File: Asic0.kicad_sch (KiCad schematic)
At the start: 18 parts, among them U2 BM1370_mode1

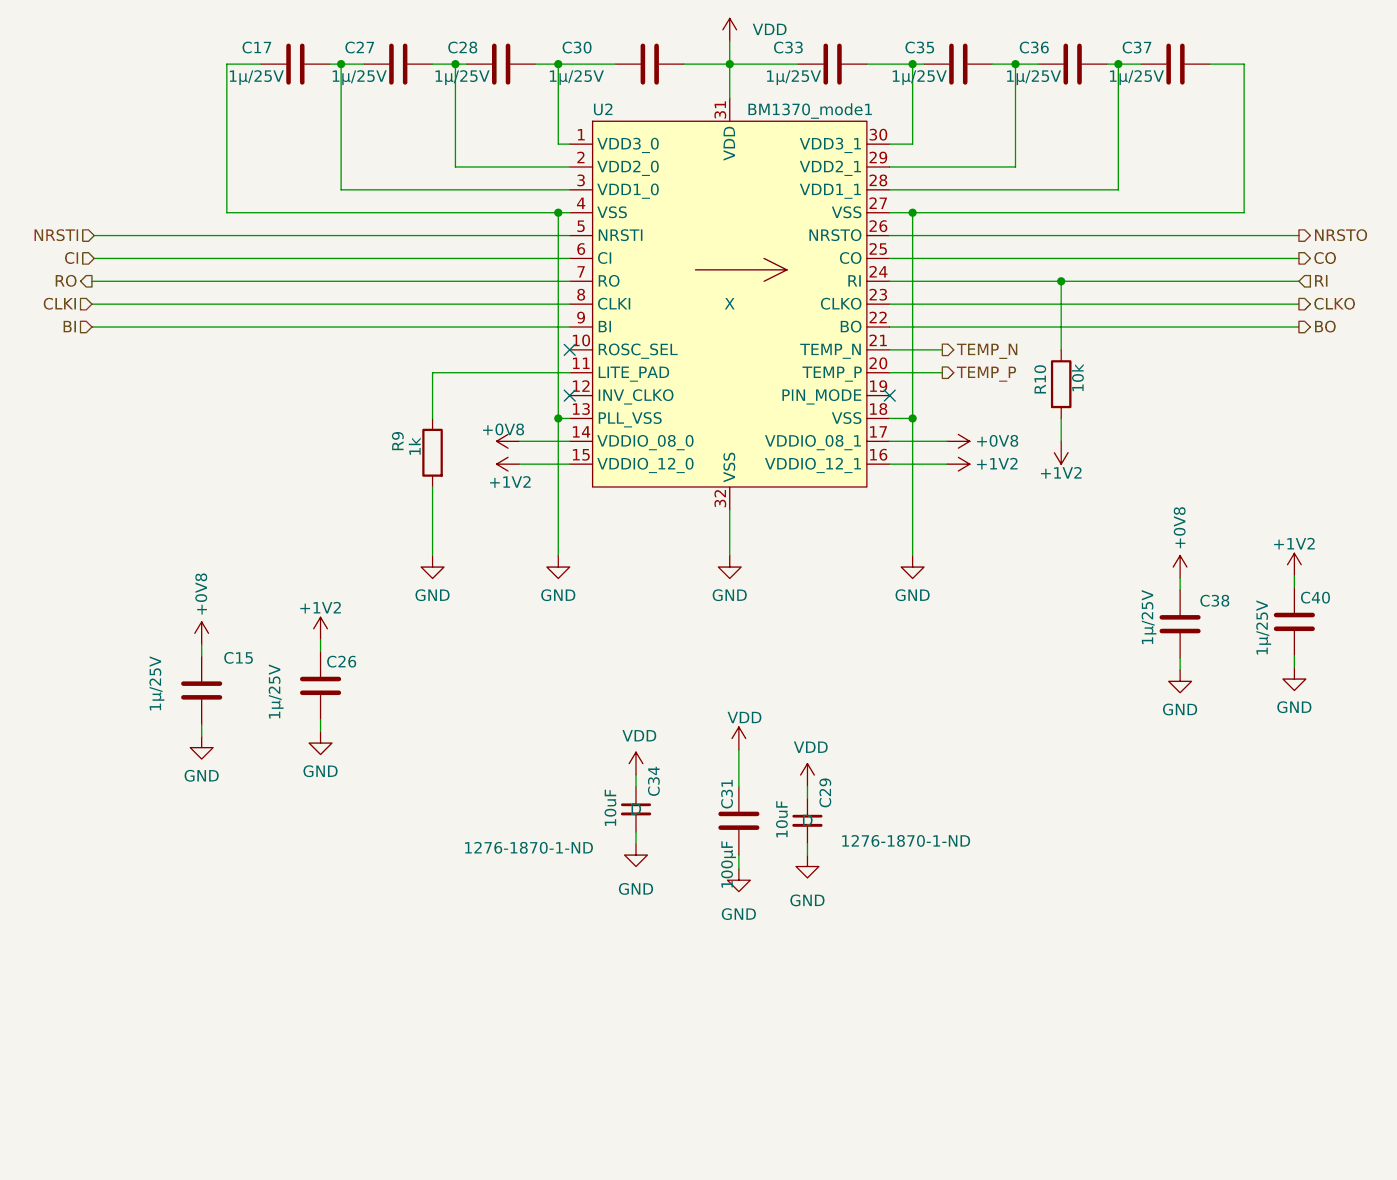
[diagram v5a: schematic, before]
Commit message: Tmux Variant
- Added curcuit to read internal Asictemps per chip
- (i)BOM changes
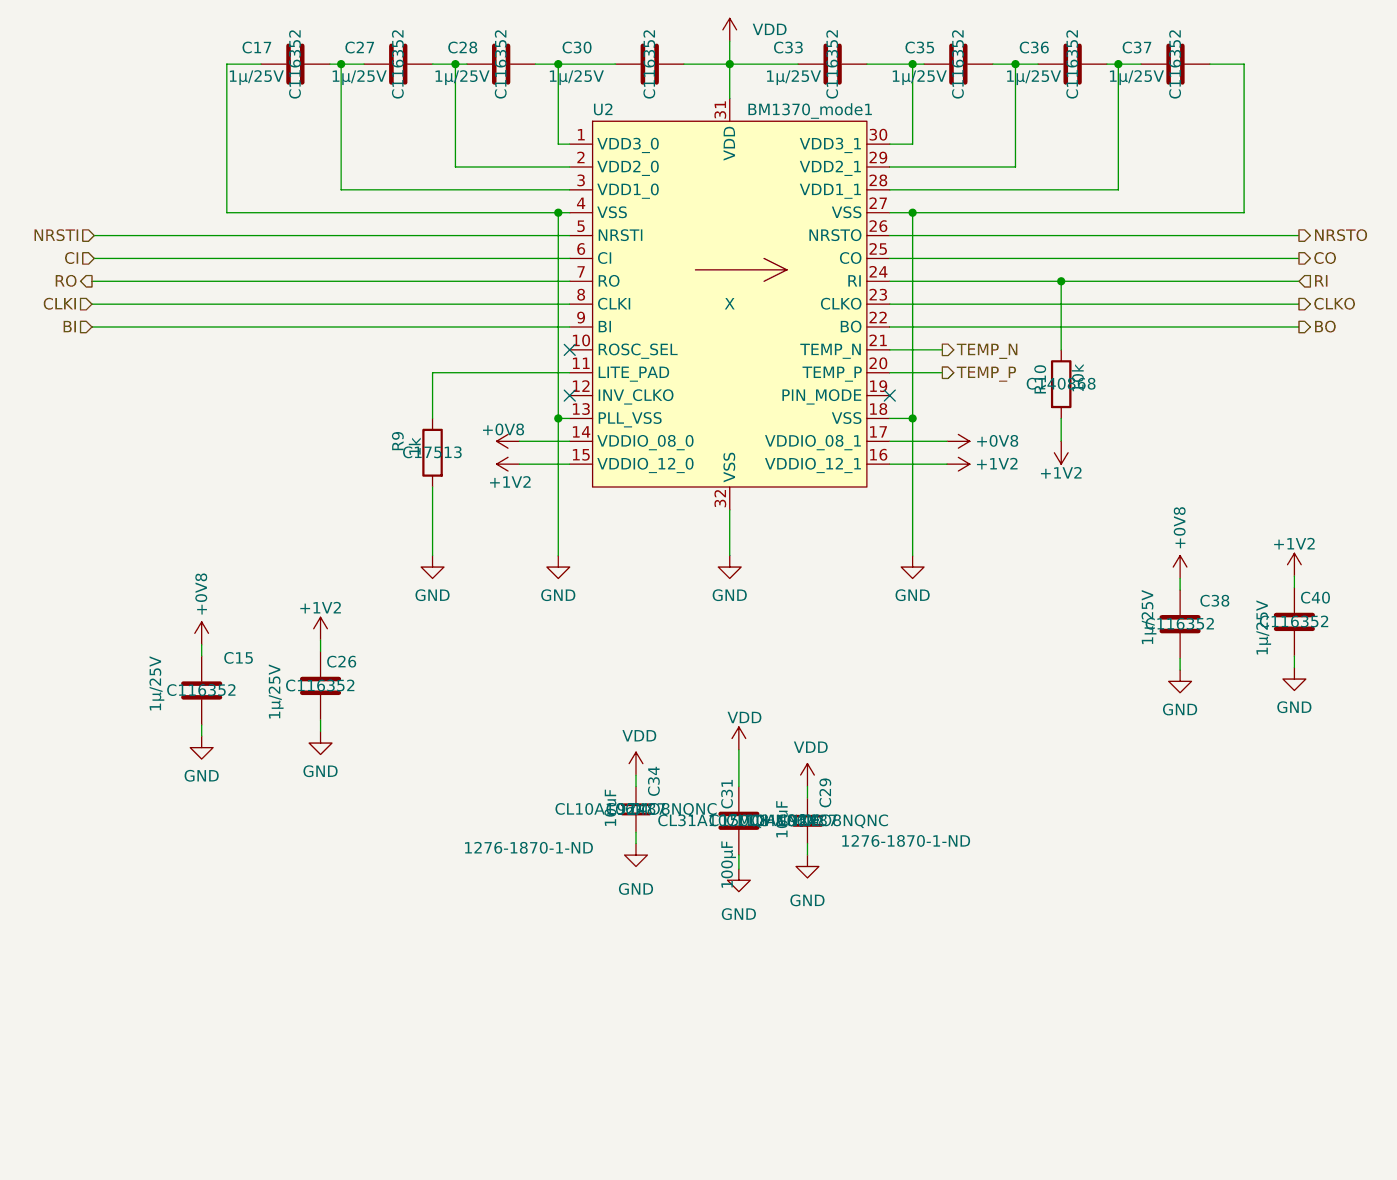
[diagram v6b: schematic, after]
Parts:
- C15, C17, C26, C27, C28, C30, C33, C35, C36, C37, C38, C40: LCSC Part # (none) -> C116352
- C29, C34: LCSC Part # (none) -> C92487; Manufacturer (none) -> CL10A106MO8NQNC
- C31: LCSC Part # (none) -> C15008; Manufacturer (none) -> CL31A107MQHNNNE; OrderNr 399-C1210C107M8PAC7800CT-ND -> 1276-1782-1-ND
- R10: LCSC Part # (none) -> C140868
- R9: LCSC Part # (none) -> C17513
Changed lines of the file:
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@@
 			)
 		)
+		(property "LCSC Part #" "C17513"
+			(at 104.394 86.106 0)
+			(effects
+				(font
+					(size 1.27 1.27)
+				)
+			)
+		)
 		(pin "1"
 		)
@@
 			)
 		)
+		(property "LCSC Part #" "C116352"
+			(at 91.948 112.014 0)
+			(effects
+				(font
+					(size 1.27 1.27)
+				)
+			)
+		)
 		(pin "1"
 		)
@@
 			)
 		)
+		(property "LCSC Part #" "C116352"
+			(at 162.814 42.926 0)
+			(effects
+				(font
+					(size 1.27 1.27)
+				)
+			)
+		)
 		(pin "1"
 		)
@@
 			)
 		)
+		(property "LCSC Part #" "C116352"
+			(at 175.514 42.926 0)
+			(effects
+				(font
+					(size 1.27 1.27)
+				)
+			)
+		)
 		(pin "1"
 		)
@@
 			)
 		)
+		(property "LCSC Part #" "C140868"
+			(at 174.244 78.486 0)
+			(effects
+				(font
+					(size 1.27 1.27)
+				)
+			)
+		)
 		(pin "1"
 		)
@@
 			)
 		)
+		(property "LCSC Part #" "C116352"
+			(at 186.944 42.926 0)
+			(effects
+				(font
+					(size 1.27 1.27)
+				)
+			)
+		)
 		(pin "1"
 		)
@@
 			)
 		)
+		(property "LCSC Part #" "C92487"
+			(at 127 125.73 0)
+			(effects
+				(font
+					(size 1.27 1.27)
+				)
+			)
+		)
+		(property "Manufacturer" "CL10A106MO8NQNC"
+			(at 127 125.73 0)
+			(effects
+				(font
+					(size 1.27 1.27)
+				)
+			)
+		)
 		(pin "1"
 		)
@@
 			)
 		)
+		(property "LCSC Part #" "C116352"
+			(at 78.74 112.522 0)
+			(effects
+				(font
+					(size 1.27 1.27)
+				)
+			)
+		)
 		(pin "1"
 		)
@@
 			)
 		)
+		(property "LCSC Part #" ""
+			(at 137.414 69.596 0)
+			(effects
+				(font
+					(size 1.27 1.27)
+				)
+			)
+		)
 		(pin "10"
 		)
@@
 			)
 		)
+		(property "LCSC Part #" "C116352"
+			(at 187.452 105.156 0)
+			(effects
+				(font
+					(size 1.27 1.27)
+				)
+			)
+		)
 		(pin "1"
 		)
@@
 			)
 		)
+		(property "LCSC Part #" "C116352"
+			(at 100.584 42.926 0)
+			(effects
+				(font
+					(size 1.27 1.27)
+				)
+			)
+		)
 		(pin "1"
 		)
@@
 			)
 		)
+		(property "LCSC Part #" "C116352"
+			(at 89.154 42.926 0)
+			(effects
+				(font
+					(size 1.27 1.27)
+				)
+			)
+		)
 		(pin "1"
 		)
@@
 			)
 		)
+		(property "LCSC Part #" "C92487"
+			(at 146.05 127 0)
+			(effects
+				(font
+					(size 1.27 1.27)
+				)
+			)
+		)
+		(property "Manufacturer" "CL10A106MO8NQNC"
+			(at 146.05 127 0)
+			(effects
+				(font
+					(size 1.27 1.27)
+				)
+			)
+		)
 		(pin "1"
 		)
@@
 			)
 		)
+		(property "LCSC Part #" "C116352"
+			(at 148.844 42.926 0)
+			(effects
+				(font
+					(size 1.27 1.27)
+				)
+			)
+		)
 		(pin "1"
 		)
@@
 			)
 		)
+		(property "LCSC Part #" "C116352"
+			(at 112.014 42.926 0)
+			(effects
+				(font
+					(size 1.27 1.27)
+				)
+			)
+		)
 		(pin "1"
 		)
@@
 			)
 		)
-		(property "OrderNr" "399-C1210C107M8PAC7800CT-ND"
+		(property "OrderNr" "1276-1782-1-ND"
 			(at 138.43 127 0)
 			(effects
@@
 			)
 		)
+		(property "Manufacturer" "CL31A107MQHNNNE"
+			(at 138.43 127 0)
+			(effects
+				(font
+					(size 1.27 1.27)
+				)
+			)
+		)
+		(property "LCSC Part #" "C15008"
+			(at 138.43 127 0)
+			(effects
+				(font
+					(size 1.27 1.27)
+				)
+			)
+		)
 		(pin "1"
 		)
@@
 			)
 		)
+		(property "LCSC Part #" "C116352"
+			(at 200.152 104.902 0)
+			(effects
+				(font
+					(size 1.27 1.27)
+				)
+			)
+		)
 		(pin "1"
 		)
@@
 			)
 		)
+		(property "LCSC Part #" "C116352"
+			(at 128.524 42.926 0)
+			(effects
+				(font
+					(size 1.27 1.27)
+				)
+			)
+		)
